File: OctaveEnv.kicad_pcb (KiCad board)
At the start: 4 copper layers, 81 parts, among them J101 IN, J102 PWR, J103 OUT, Q101 BC857, SW101 Stomp, U101 AZ34063U, U102 L7805, U103 TL074, U104 74HCT74, U105 LM13700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

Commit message: layout done
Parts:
- C102, C103, C125, R123, R124, R131, U102: moved to B.Cu
- moved D104 359.9 mm to (6.25, 26.8)
- moved D105 355.0 mm to (10.3, 40.3), turned to 90 degrees
- moved U106 345.7 mm to (12.0, 32.7)
- moved R119 342.5 mm to (6.22, 37.4)
- moved C116 341.2 mm to (6.28, 32.7), turned to 180 degrees
- moved Q101 338.1 mm to (20.1, 24.4), turned to 90 degrees
- moved R113 337.1 mm to (6.25, 30.3)
- moved C125 335.2 mm to (16.7, 40.4), turned to 90 degrees
- moved R130 335.2 mm to (17.1, 35.7), turned to -90 degrees
- moved R123 334.7 mm to (13.4, 40.4), turned to 90 degrees
- moved C123 333.4 mm to (18.4, 28.4), turned to 90 degrees
- moved R127 332.4 mm to (20.6, 35.7), turned to -90 degrees
- moved C117 329.8 mm to (17.6, 32.7)
- moved R124 327.9 mm to (20.0, 40.3), turned to 90 degrees
- moved R118 326.4 mm to (21.8, 28.4), turned to 90 degrees
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
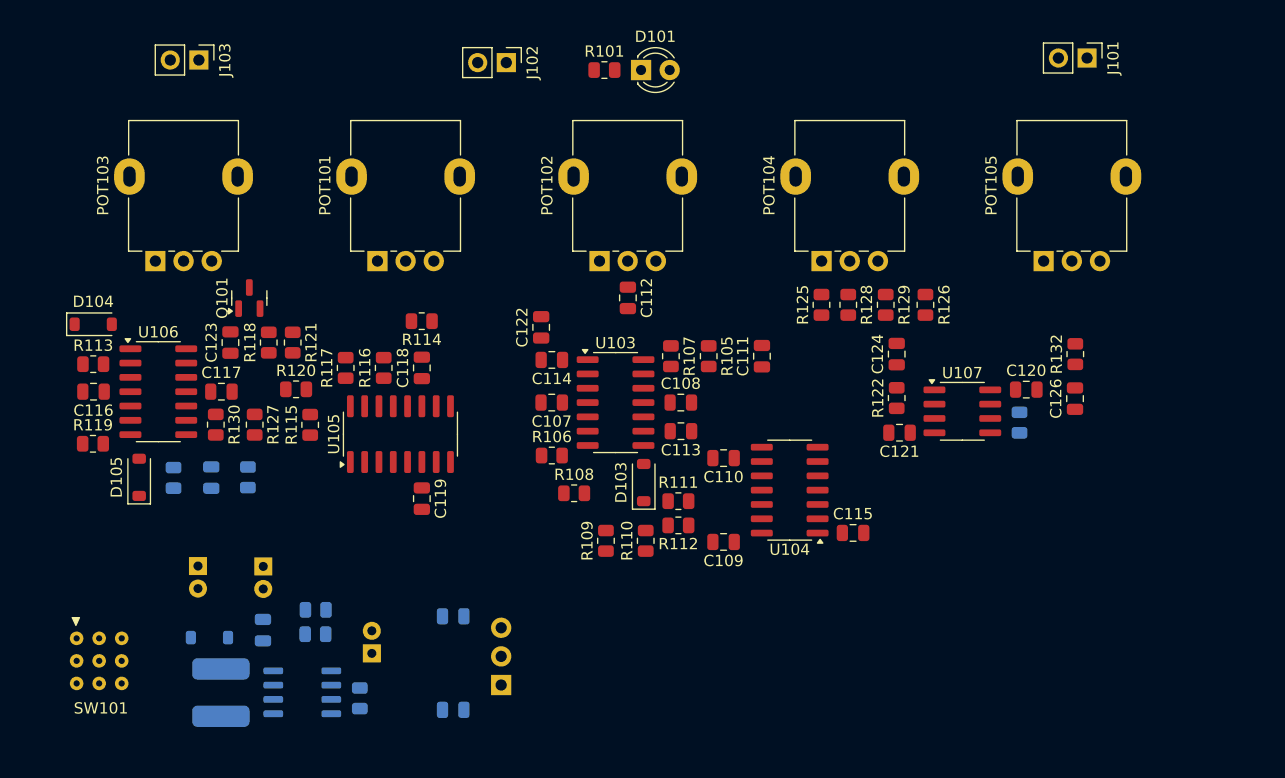
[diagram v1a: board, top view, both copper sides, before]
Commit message: routing and test points
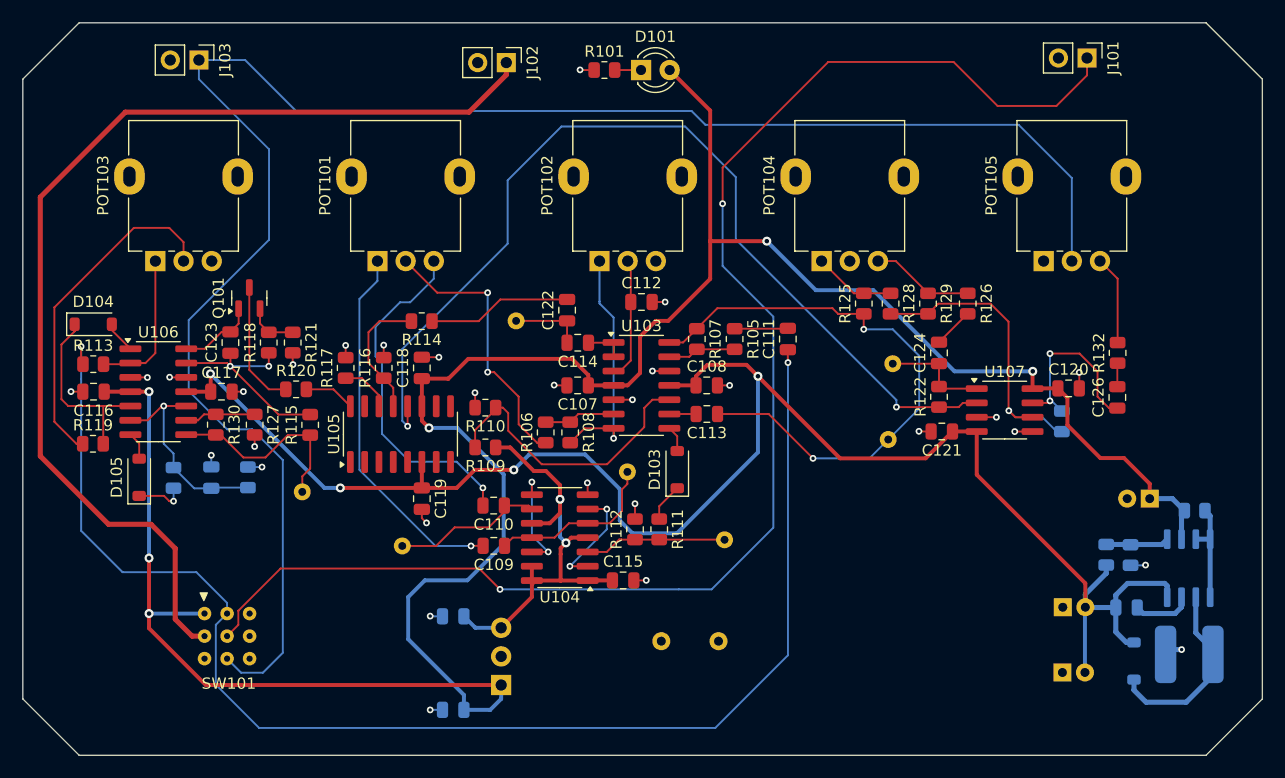
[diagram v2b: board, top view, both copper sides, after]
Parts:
- added R133: LOOP, Resistor_THT:R_Axial_DIN0207_L6.3mm_D2.5mm_P5.08mm_Vertical, B.Cu at (56.7, 54.9)
- added TP101: GTR GAIN, TestPoint:TestPoint_THTPad_D1.5mm_Drill0.7mm_VAL, B.Cu at (76.8, 37.0)
- added TP102: ENV, TestPoint:TestPoint_THTPad_D1.5mm_Drill0.7mm_VAL, B.Cu at (24.8, 41.6)
- added TP103: VCA IN, TestPoint:TestPoint_THTPad_D1.5mm_Drill0.7mm_VAL, B.Cu at (43.8, 26.4)
- added TP104: VCA_OUT, TestPoint:TestPoint_THTPad_D1.5mm_Drill0.7mm_VAL, B.Cu at (77.2, 30.2)
- added TP105: EDGE, TestPoint:TestPoint_THTPad_D1.5mm_Drill0.7mm_VAL, B.Cu at (62.3, 45.9)
- added TP106: SQR1, TestPoint:TestPoint_THTPad_D1.5mm_Drill0.7mm_VAL, B.Cu at (53.6, 39.9)
- added TP107: SQR2, TestPoint:TestPoint_THTPad_D1.5mm_Drill0.7mm_VAL, B.Cu at (33.7, 46.4)
- moved L101 86.0 mm to (103.5, 56.0), turned to 180 degrees
- moved D102 82.1 mm to (98.6, 56.6), turned to 90 degrees
- moved U101 79.4 mm to (103.5, 48.4), turned to 90 degrees
- moved C106 77.3 mm to (92.3, 57.7), turned to 0 degrees
- moved C104 76.7 mm to (97.9, 51.9), turned to 180 degrees
- moved R102 75.9 mm to (104.0, 43.3), turned to 0 degrees
- moved R103 72.7 mm to (98.3, 47.2), turned to 90 degrees
- moved C105 71.0 mm to (92.3, 51.9), turned to 0 degrees
- moved C101 70.4 mm to (100.0, 42.2), turned to 180 degrees
- moved R104 70.3 mm to (96.1, 47.2), turned to -90 degrees
- moved U104 20.8 mm to (47.6, 45.7)
- moved C110 20.8 mm to (41.8, 42.8)
- moved C115 20.8 mm to (53.3, 49.5)
- moved C109 20.4 mm to (41.8, 46.4)
- moved R110 18.5 mm to (41.0, 34.1), turned to 180 degrees
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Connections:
- SW101 pad 2: Net-(J102-Pin_1) -> FX_IN
- SW101 pad 4: FX_IN -> Net-(J102-Pin_1)
- SW101 pad 6: JACK_OUT -> unconnected-(SW101C-COMC-Pad6)
- SW101 pad 8: unconnected-(SW101C-COMC-Pad8) -> JACK_OUT
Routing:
- net +9V: track 0.00 -> 221.3 mm, vias 0 -> 6
- net JACK_OUT: track 0.00 -> 158.3 mm
- net -9V: track 0.00 -> 151.3 mm, vias 0 -> 4
- net JACK_IN: track 0.00 -> 129.0 mm, vias 0 -> 2
- net FX_IN: track 0.00 -> 123.4 mm, vias 0 -> 2
- net Net-(J102-Pin_1): track 0.00 -> 94.8 mm
- net Net-(U107A--): track 0.00 -> 85.4 mm, vias 0 -> 2
- net GTR_GAIN: track 0.00 -> 52.0 mm, vias 0 -> 2
- net +5V: track 0.00 -> 39.8 mm, vias 0 -> 2
- net GND: track 0.00 -> 38.0 mm, vias 0 -> 30
- net Net-(C109-Pad2): track 0.00 -> 33.0 mm, vias 0 -> 1
- net Net-(C110-Pad2): track 0.00 -> 30.7 mm, vias 0 -> 1
- net Net-(POT103-Pad2): track 0.00 -> 30.1 mm
- net Net-(U107B--): track 0.00 -> 27.2 mm, vias 0 -> 1
- net Net-(U103C-+): track 0.00 -> 26.1 mm
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- added copper zone on In1.Cu, net GND
- added copper zone on In2.Cu, net GND
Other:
- board outline added: 110 x 65 mm

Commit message: smaller outline
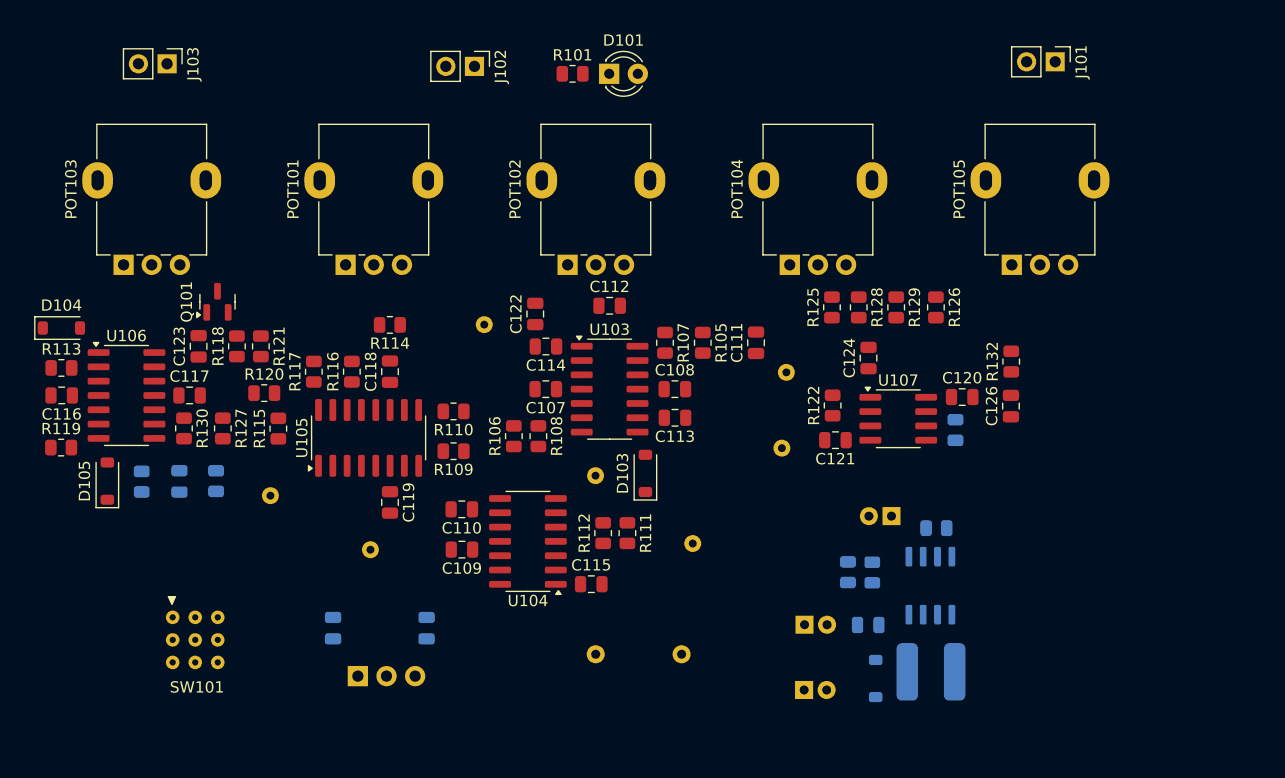
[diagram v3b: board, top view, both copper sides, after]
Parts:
- R133: footprint Resistor_THT:R_Axial_DIN0207_L6.3mm_D2.5mm_P5.08mm_Vertical -> Resistor_THT:R_Axial_DIN0207_L6.3mm_D2.5mm_P7.62mm_Horizontal
- moved C105 23.0 mm to (69.4, 53.4)
- moved U101 23.0 mm to (80.5, 50.0)
- moved R103 23.0 mm to (75.4, 48.8)
- moved C101 23.0 mm to (77.1, 43.8)
- moved C104 23.0 mm to (75.0, 53.4)
- moved C106 23.0 mm to (69.3, 59.2)
- moved D102 23.0 mm to (75.7, 58.2)
- moved L101 23.0 mm to (80.6, 57.6)
- moved R102 23.0 mm to (81.1, 44.8)
- moved R104 23.0 mm to (73.2, 48.8)
- moved C102 12.9 mm to (27.5, 53.7), turned to 90 degrees
- moved U102 10.3 mm to (32.3, 58.0), turned to 0 degrees
- moved C120 9.47 mm to (83.4, 33.2)
- moved C121 9.47 mm to (72.1, 37.0)
- moved C126 9.47 mm to (87.7, 34.0)
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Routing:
- net +9V: track 221.3 -> 0.00 mm, vias 6 -> 0
- net JACK_OUT: track 158.3 -> 0.00 mm
- net -9V: track 151.3 -> 0.00 mm, vias 4 -> 0
- net JACK_IN: track 129.0 -> 0.00 mm, vias 2 -> 0
- net FX_IN: track 123.4 -> 0.00 mm, vias 2 -> 0
- net Net-(J102-Pin_1): track 94.8 -> 0.00 mm
- net Net-(U107A--): track 85.4 -> 0.00 mm, vias 2 -> 0
- net GTR_GAIN: track 52.0 -> 0.00 mm, vias 2 -> 0
- net +5V: track 39.8 -> 0.00 mm, vias 2 -> 0
- net GND: track 38.0 -> 0.00 mm, vias 30 -> 0
- net Net-(C109-Pad2): track 33.0 -> 0.00 mm, vias 1 -> 0
- net Net-(C110-Pad2): track 30.7 -> 0.00 mm, vias 1 -> 0
- net Net-(POT103-Pad2): track 30.1 -> 0.00 mm
- net Net-(U107B--): track 27.2 -> 0.00 mm, vias 1 -> 0
- net Net-(U103C-+): track 26.1 -> 0.00 mm
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- removed copper zone on In1.Cu, net GND
- removed copper zone on In2.Cu, net GND
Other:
- board outline removed

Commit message: silkscreen stuff, new layout
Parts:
- moved J102 56.2 mm to (46.1, 59.8)
- moved R132 25.1 mm to (64.8, 40.3), turned to -90 degrees
- moved C126 23.0 mm to (64.8, 36.3), turned to -90 degrees
- moved TP104 17.7 mm to (84.3, 37.3), turned to -90 degrees
- moved C120 14.8 mm to (69.1, 37.1), turned to 180 degrees
- moved C112 13.6 mm to (41.6, 33.8), turned to -90 degrees
- moved R131 13.3 mm to (69.7, 34.0), turned to -90 degrees
- moved R102 13.2 mm to (82.3, 58.0), turned to -90 degrees
- moved C106 13.0 mm to (68.0, 46.3), turned to -90 degrees
- moved C101 12.0 mm to (83.4, 54.0), turned to 90 degrees
- moved C124 11.1 mm to (77.4, 40.6), turned to -90 degrees
- moved L101 11.0 mm to (69.6, 57.5), turned to 90 degrees
- moved J103 10.5 mm to (23.1, 5.55)
- moved J101 9.84 mm to (82.0, 5.70)
- moved R122 9.09 mm to (80.6, 36.4), turned to -90 degrees
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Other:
- board outline added: 100 x 65 mm
- board text added: "+"
- board text added: "1/2 Blend"
- board text added: "Env. Gain"
- board text added: "In"
- board text added: "Out"
- board text added: "Power"
- board text added: "Tone"
- board text added: "Volume"
- board text added: "Wet/Dry"

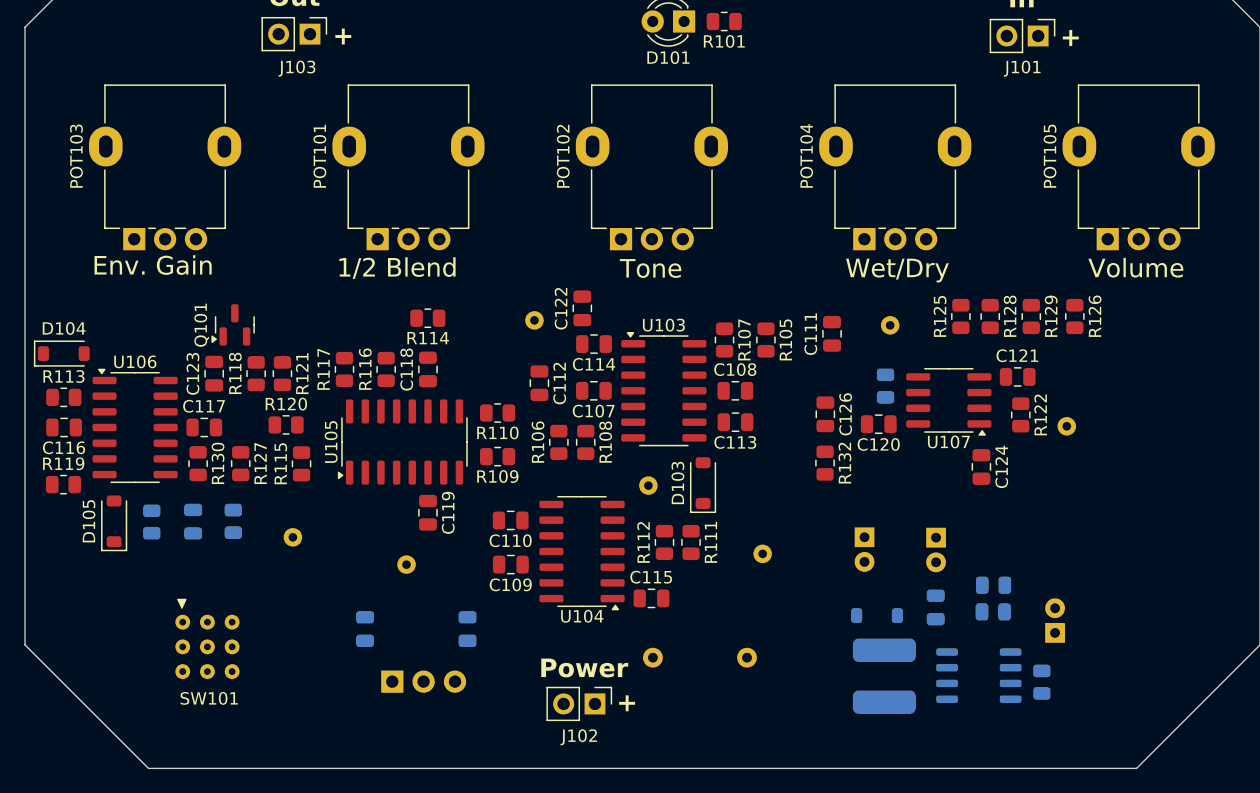
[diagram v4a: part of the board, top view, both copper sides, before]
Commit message: new routing started
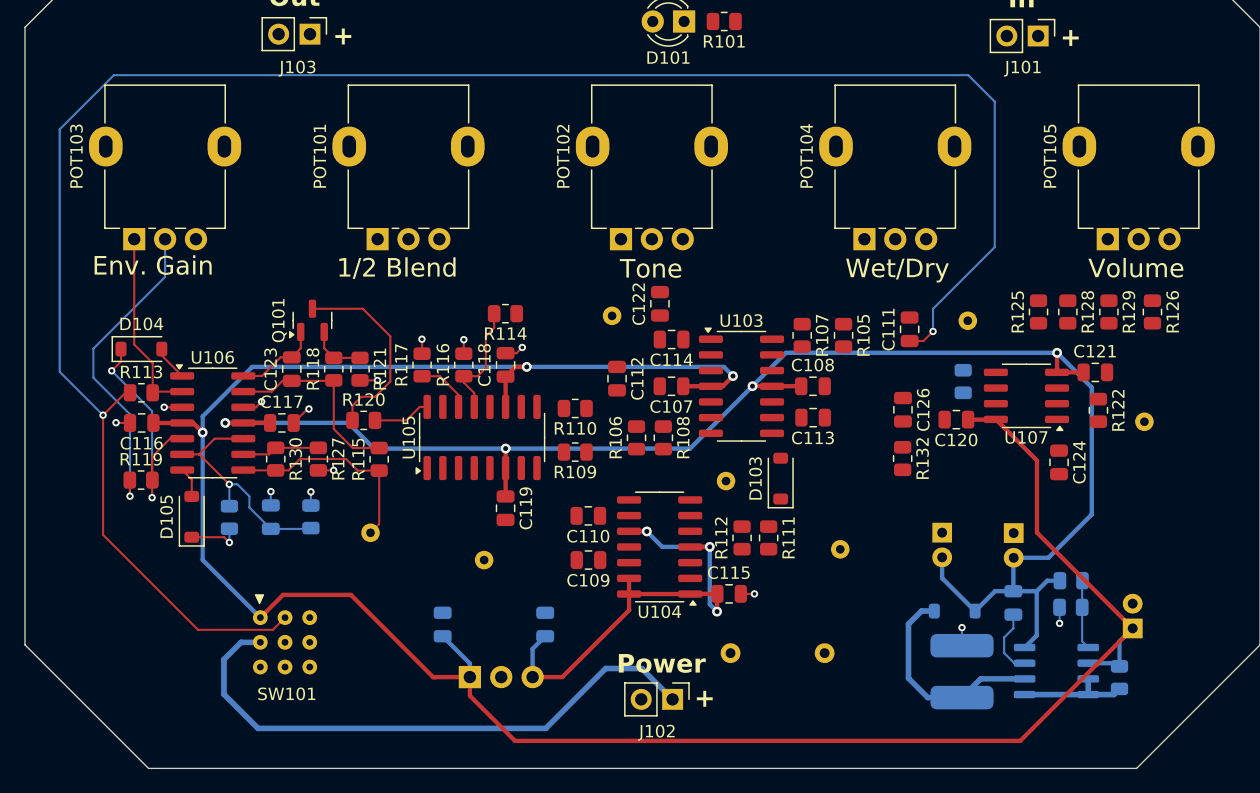
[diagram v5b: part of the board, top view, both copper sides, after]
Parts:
- moved C101 6.30 mm to (89.7, 53.7)
- moved C111 6.30 mm to (71.6, 29.4)
- moved R103 6.30 mm to (84.7, 52.0)
- moved R129 6.30 mm to (87.8, 28.0)
- moved TP104 6.30 mm to (90.6, 36.9)
- moved C108 6.30 mm to (63.8, 34.1)
- moved C112 6.30 mm to (47.9, 33.4)
- moved C115 6.30 mm to (57.0, 50.9)
- moved D103 6.30 mm to (61.2, 41.5)
- moved J102 6.30 mm to (52.4, 59.4)
- moved R105 6.30 mm to (66.3, 29.9)
- moved R106 6.30 mm to (49.5, 38.2)
- moved R107 6.30 mm to (62.9, 29.9)
- moved R108 6.30 mm to (51.7, 38.2)
- moved R112 6.30 mm to (58.1, 46.3)
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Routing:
- net +9V: track 0.00 -> 191.4 mm, vias 0 -> 3
- net FX_IN: track 0.00 -> 156.9 mm, vias 0 -> 2
- net -9V: track 0.00 -> 129.7 mm, vias 0 -> 4
- net Net-(J102-Pin_1): track 0.00 -> 46.9 mm
- net +5V: track 0.00 -> 39.1 mm, vias 0 -> 3
- net Net-(POT103-Pad2): track 0.00 -> 25.8 mm, vias 0 -> 1
- net Net-(D104-K): track 0.00 -> 20.1 mm, vias 0 -> 2
- net Net-(U106B--): track 0.00 -> 19.4 mm, vias 0 -> 1
- net GND: track 0.00 -> 18.6 mm, vias 0 -> 14
- net Net-(D102-K): track 0.00 -> 17.6 mm
- net ENV: track 0.00 -> 17.1 mm
- net Net-(Q101-C): track 0.00 -> 16.0 mm
- net Net-(U106D--): track 0.00 -> 15.9 mm
- net Net-(U106A--): track 0.00 -> 15.5 mm
- net Net-(U105A--): track 0.00 -> 10.3 mm
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- added copper zone on In1.Cu, net GND
- added copper zone on In2.Cu, net GND
